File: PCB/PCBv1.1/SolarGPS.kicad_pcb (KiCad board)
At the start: 2 copper layers, 75 x 27 mm, 56 parts, among them J1 Conn_01x10_Female, J2 Solar1+, J3 GND, J4 Conn_02x03_Odd_Even, J5 Solar2+, J6 GND, J7 Screw_Terminal_01x01, U1 STM32L011G3Ux, U2 MAX-M10Q, U5 BQ25505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

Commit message: Remove control app
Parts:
- R4: value 412k -> 432k
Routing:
- net GND: track 11.1 -> 9.68 mm

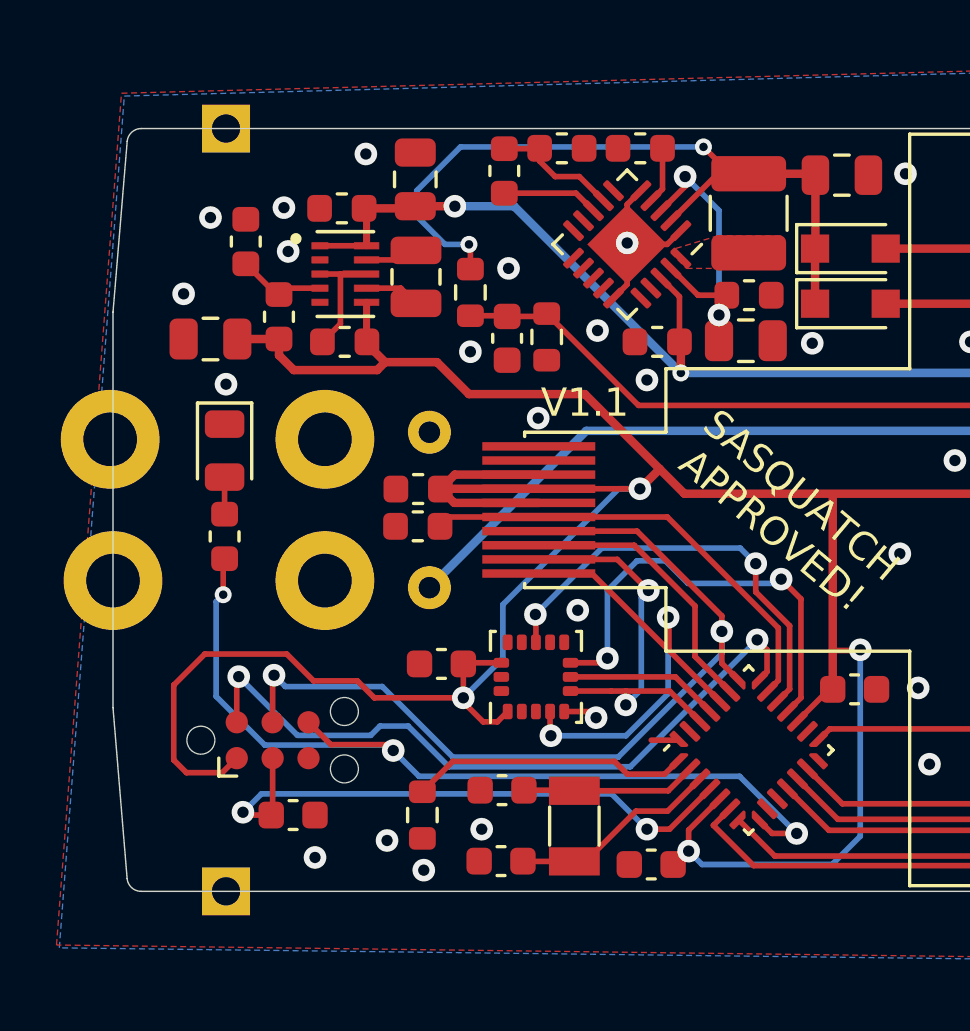
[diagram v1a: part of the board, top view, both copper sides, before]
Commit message: Add custom library revise M4 mount
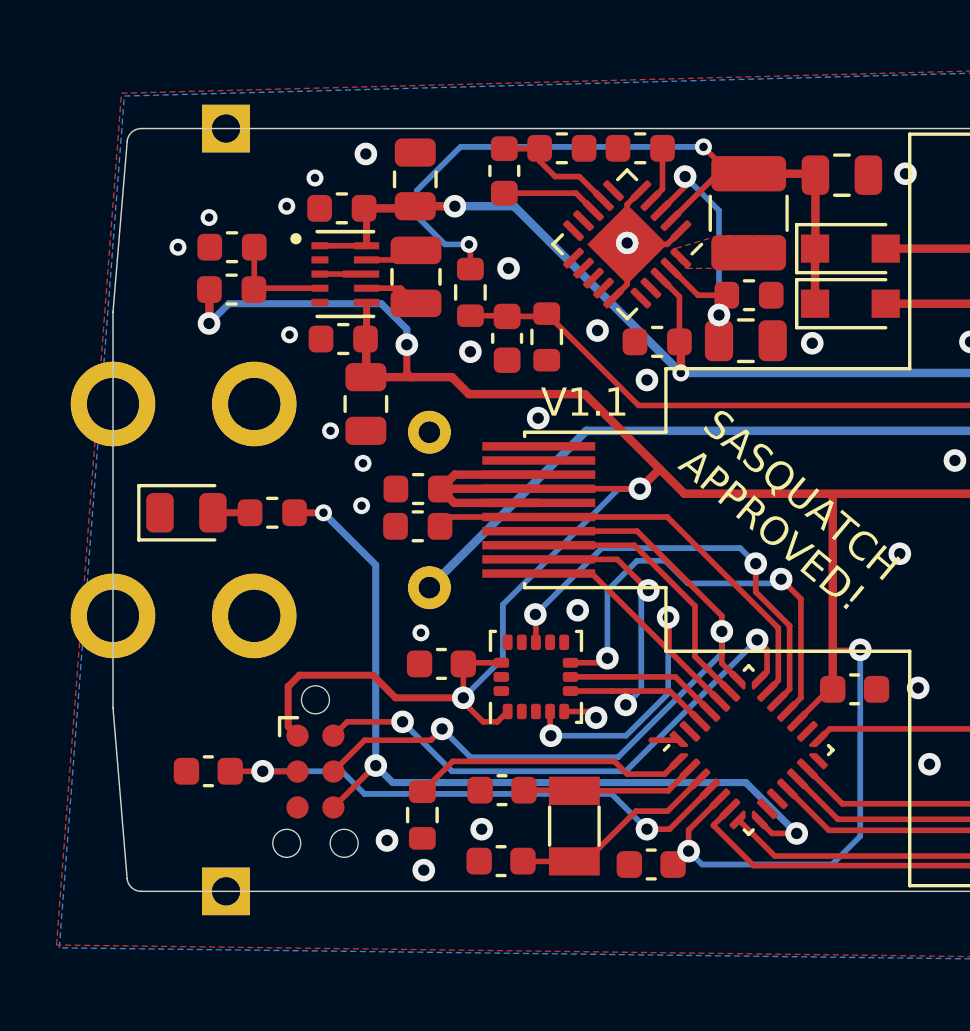
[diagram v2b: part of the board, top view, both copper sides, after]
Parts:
- J7: footprint Veridian-Library-KiCad:Right Angle Screw Terminal M3M4 -> Heliograph:M4_RA_7792
- moved C7 5.96 mm to (58.0, 59.8), turned to 90 degrees
- moved C18 3.38 mm to (52.4, 72.8), turned to 0 degrees
- moved D2 2.58 mm to (51.6, 63.6), turned to 0 degrees
- moved R4 1.93 mm to (53.2, 55.7), turned to 180 degrees
- moved R3 1.88 mm to (54.6, 63.6), turned to 180 degrees
- moved J4 1.88 mm to (56.2, 72.8), turned to -90 degrees
- moved R5 0.53 mm to (53.2, 54.2), turned to 0 degrees
- moved C5 0.11 mm to (57.1, 57.5)
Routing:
- net /SWDIO: track 25.1 -> 19.5 mm
- net EXTCOMIN: track 31.3 -> 27.3 mm
- net VDD: track 147.4 -> 144.6 mm, vias 4 -> 6
- net GND: track 9.68 -> 7.37 mm, vias 59 -> 62
- net LED: track 32.5 -> 30.3 mm
- net RESET: track 21.0 -> 19.7 mm
- net Net-(R4-Pad1): track 3.17 -> 3.86 mm

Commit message: Update PCB 1.1
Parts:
- C12, C7: footprint Capacitor_SMD:C_0805_2012Metric -> Capacitor_SMD:C_1206_3216Metric
- moved C12 1.94 mm to (57.9, 51.2), turned to 0 degrees
- moved C7 0.81 mm to (57.4, 60.4)
- moved C8 0.12 mm to (57.1, 53.0)
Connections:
- U1 pad 28: GND -> unconnected-(U1-Pad28)
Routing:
- net VBAT: track 76.1 -> 77.8 mm
- net GND: track 7.37 -> 8.96 mm, vias 62 -> 61
- net SOLAR+: track 27.2 -> 26.5 mm

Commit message: Tweak PCB
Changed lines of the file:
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@@
   (via (at 87.75 60.65) (size 0.8) (drill 0.4) (layers "F.Cu" "B.Cu") (free) (net 1))
   (via (at 55.25 57.3) (size 0.6) (drill 0.3) (layers "F.Cu" "B.Cu") (free) (net 1))
-  (via (at 62.05 74.8) (size 0.8) (drill 0.4) (layers "F.Cu" "B.Cu") (free) (net 1))
+  (via (at 61.95 74.65) (size 0.8) (drill 0.4) (layers "F.Cu" "B.Cu") (free) (net 1))
   (via (at 57.8 63.35) (size 0.6) (drill 0.3) (layers "F.Cu" "B.Cu") (free) (net 1))
   (via (at 106.6 74.15) (size 0.8) (drill 0.4) (layers "F.Cu" "B.Cu") (free) (net 1))

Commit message: Revise
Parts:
- C14, C17: value 10F -> 15F; footprint Veridian-Library-KiCad:SCCT20E106SRB -> Heliograph:SCCT30E156SRB
- moved C14 7.10 mm to (90.0, 63.5)
- moved C17 3.20 mm to (57.0, 63.5)
- moved C7 2.47 mm to (59.7, 59.5)
- moved C26 0.82 mm to (60.8, 68.2)
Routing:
- net LED: track 30.3 -> 37.4 mm
- net SOLAR_SENSE1: track 60.4 -> 65.1 mm
- net VBATMID: track 61.1 -> 64.2 mm
- net VDD: track 144.6 -> 142.5 mm
- net VBAT: track 77.8 -> 76.1 mm
- net GND: vias 61 -> 56
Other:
- board text added: "GPS GALILEO GLONASS BEIDOU"
- board text removed: "GNSS"
